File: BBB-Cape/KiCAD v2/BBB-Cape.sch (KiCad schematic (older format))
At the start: 8 parts, among them J1 MOUNTING_HOLE, J2 MOUNTING_HOLE, J3 MOUNTING_HOLE, J4 MOUNTING_HOLE, J5 MOUNTING_HOLE, J6 MOUNTING_HOLE, J7 MOUNTING_HOLE, J8 MOUNTING_HOLE

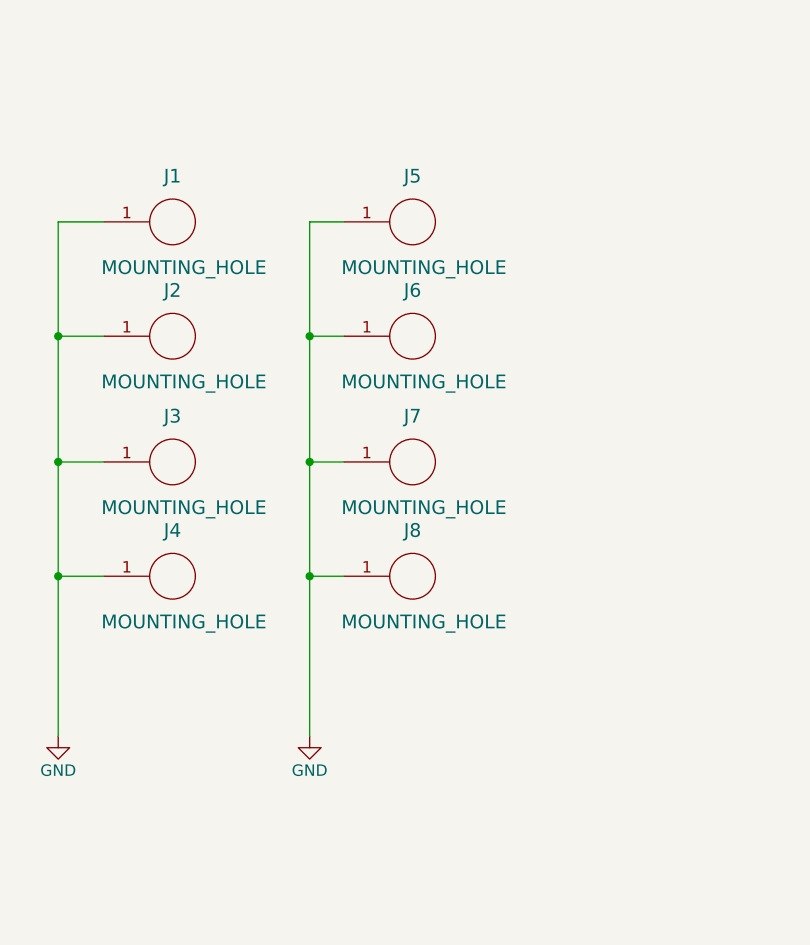
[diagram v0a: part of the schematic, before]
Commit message: Layout Fix
Updated a few footprints, fixed the positioning of P8 and P9, and adjusted general layout a bit.
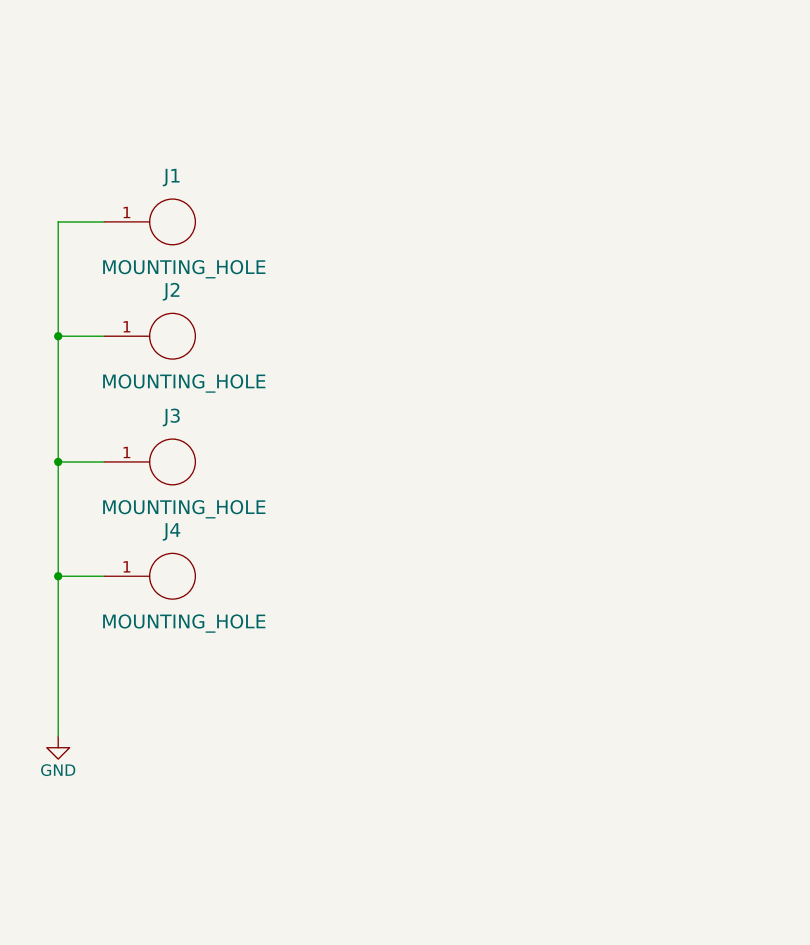
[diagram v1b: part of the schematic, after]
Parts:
- removed J5, J6, J7, J8: MOUNTING_HOLE, Mounting_Holes:MountingHole_3.2mm_M3_Pad, symbol MOUNTING_HOLE
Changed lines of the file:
@@
-$EndComp
-$Comp
-L MOUNTING_HOLE J5
-U 1 1 5A373A79
-P 9600 3050
-F 0 "J5" H 9700 3250 60  0000 C CNN
-F 1 "MOUNTING_HOLE" H 9750 2850 60  0000 C CNN
-F 2 "Mounting_Holes:MountingHole_3.2mm_M3_Pad" H 9600 3050 60  0001 C CNN
-F 3 "" H 9600 3050 60  0001 C CNN
-	1    9600 3050
-	1    0    0    -1
-$EndComp
-$Comp
-L MOUNTING_HOLE J6
-U 1 1 5A373A7F
-P 9600 3550
-F 0 "J6" H 9700 3750 60  0000 C CNN
-F 1 "MOUNTING_HOLE" H 9750 3350 60  0000 C CNN
-F 2 "Mounting_Holes:MountingHole_3.2mm_M3_Pad" H 9600 3550 60  0001 C CNN
-F 3 "" H 9600 3550 60  0001 C CNN
-	1    9600 3550
-	1    0    0    -1
-$EndComp
-$Comp
-L MOUNTING_HOLE J7
-U 1 1 5A373A85
-P 9600 4100
-F 0 "J7" H 9700 4300 60  0000 C CNN
-F 1 "MOUNTING_HOLE" H 9750 3900 60  0000 C CNN
-F 2 "Mounting_Holes:MountingHole_3.2mm_M3_Pad" H 9600 4100 60  0001 C CNN
-F 3 "" H 9600 4100 60  0001 C CNN
-	1    9600 4100
-	1    0    0    -1
-$EndComp
-$Comp
-L MOUNTING_HOLE J8
-U 1 1 5A373A8B
-P 9600 4600
-F 0 "J8" H 9700 4800 60  0000 C CNN
-F 1 "MOUNTING_HOLE" H 9750 4400 60  0000 C CNN
-F 2 "Mounting_Holes:MountingHole_3.2mm_M3_Pad" H 9600 4600 60  0001 C CNN
-F 3 "" H 9600 4600 60  0001 C CNN
-	1    9600 4600
-	1    0    0    -1
-$EndComp
-$Comp
-L GND #PWR01
-U 1 1 5A373AAB
-P 9250 5300
-F 0 "#PWR01" H 9250 5050 50  0001 C CNN
-F 1 "GND" H 9250 5150 50  0000 C CNN
-F 2 "" H 9250 5300 50  0001 C CNN
-F 3 "" H 9250 5300 50  0001 C CNN
-	1    9250 5300
-	1    0    0    -1
 $EndComp
 $Comp
@@
 $EndComp
 Wire Wire Line
-	9400 3050 9250 3050
-Wire Wire Line
-	9250 3050 9250 5300
-Wire Wire Line
-	9400 3550 9250 3550
-Connection ~ 9250 3550
-Wire Wire Line
-	9400 4100 9250 4100
-Connection ~ 9250 4100
-Wire Wire Line
-	9400 4600 9250 4600
-Connection ~ 9250 4600
-Wire Wire Line
 	8350 3050 8150 3050
